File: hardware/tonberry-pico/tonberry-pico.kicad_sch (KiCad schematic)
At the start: 28 parts, among them J1 MicroSD_Breakout, J2 SparkFun I2S Audio Breakout M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, J3 RC522_Breakout, J4 Adafruit_bq25185_5V, J5 UART, J6 WS2812, J7 Buttons, Q1 2N7000, Q2 2N7000, SW1 SW_Push, SW2 SW_Push, SW3 SW_Push, SW4 SW_Push, SW5 SW_Push, U1 Pico

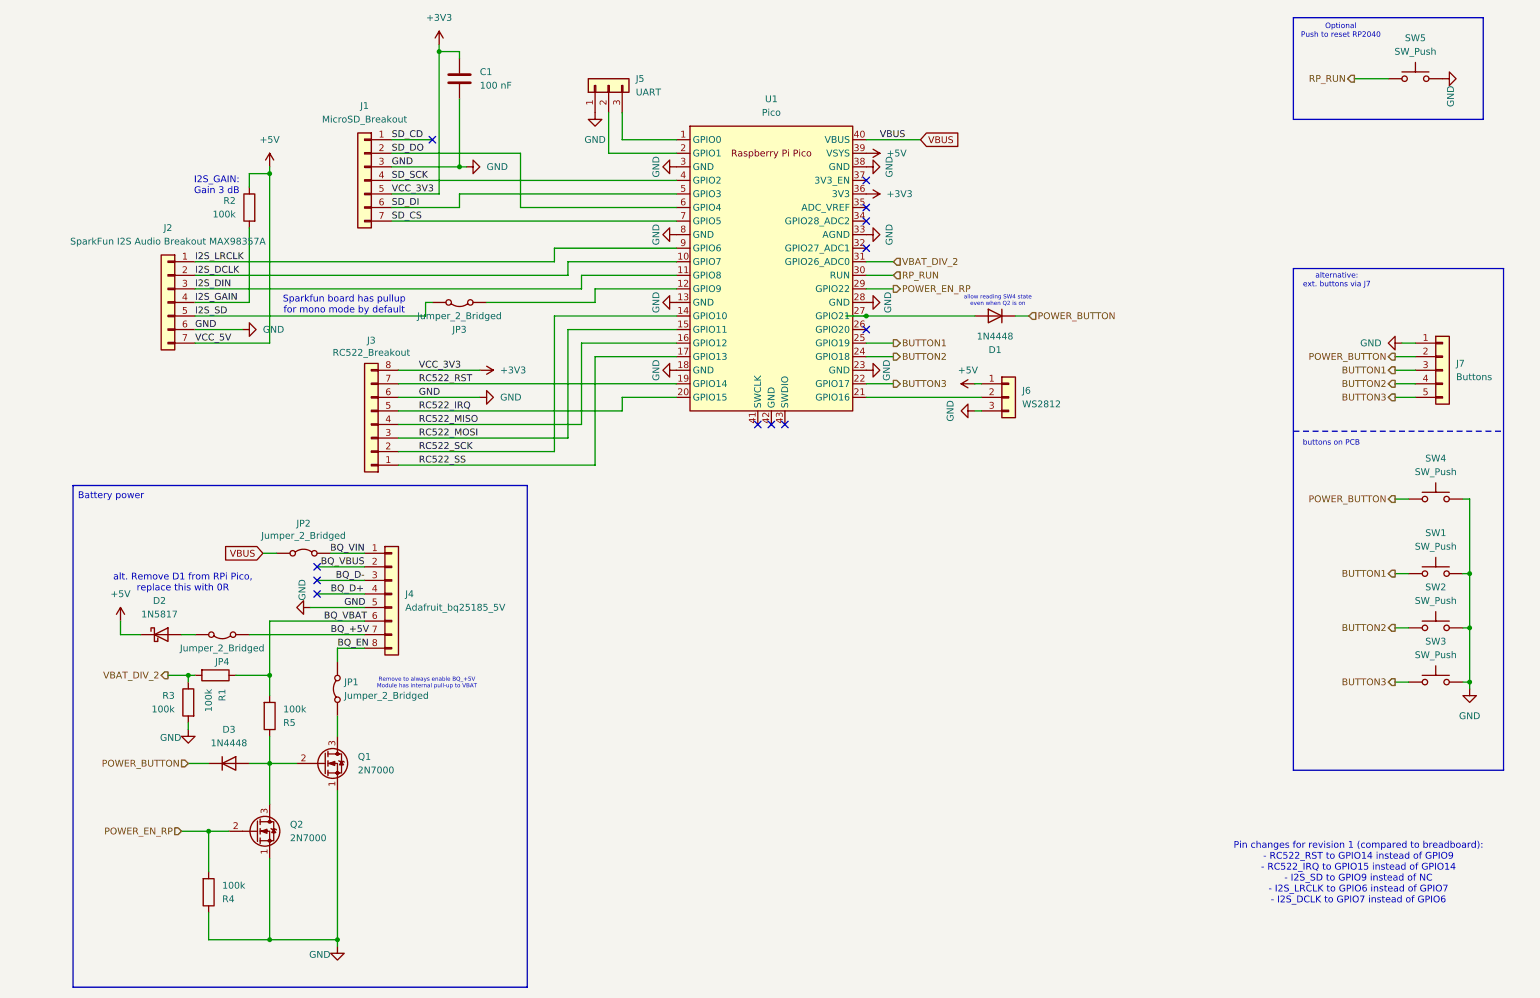
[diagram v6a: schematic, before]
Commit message: hw: Use new and improved RPi Pico symbol in schematic
Signed-off-by: Matthias Blankertz <matthias@blankertz.org>
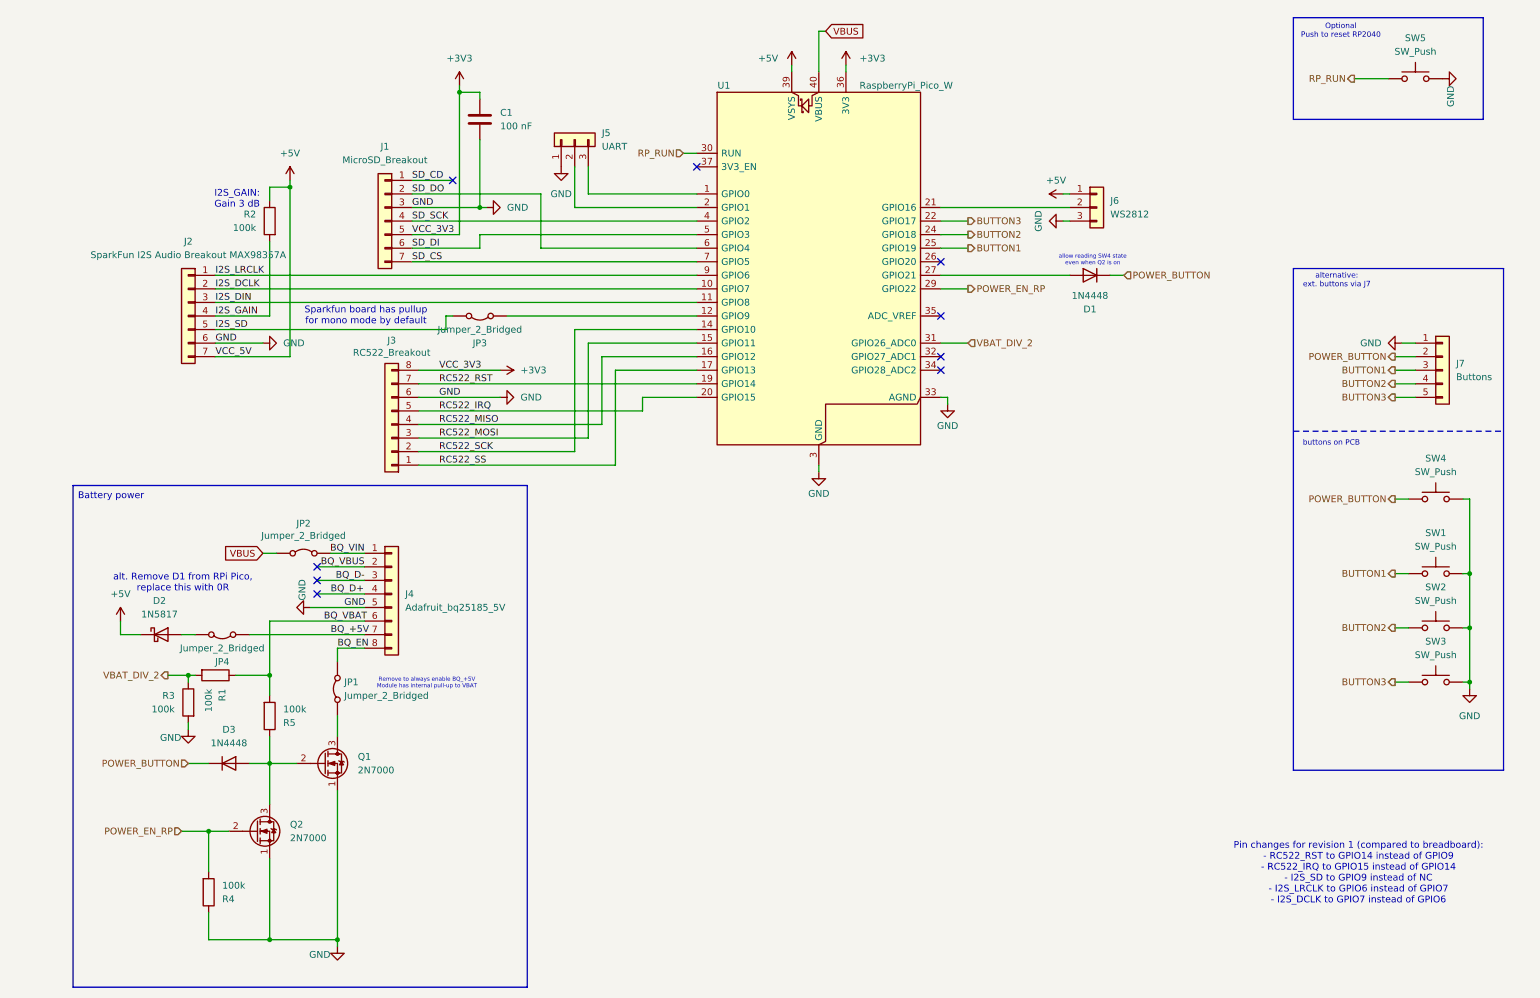
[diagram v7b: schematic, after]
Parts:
- SW5: footprint Button_Switch_THT:Push_E-Switch_KS01Q01 -> Connector_PinHeader_2.54mm:PinHeader_1x02_P2.54mm_Vertical
- U1: value Pico -> RaspberryPi_Pico_W; symbol MCU_RaspberryPi_and_Boards:Pico -> MCU_Module:RaspberryPi_Pico_W
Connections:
- no-connect marks 12 -> 9
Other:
- moved on the sheet: C1, D1, J1, J2, J3, J5, J6, JP3, R2

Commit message: hw: Cleanup schematic style, fix ERC violations
No netlist changes.

Signed-off-by: Matthias Blankertz <matthias@blankertz.org>
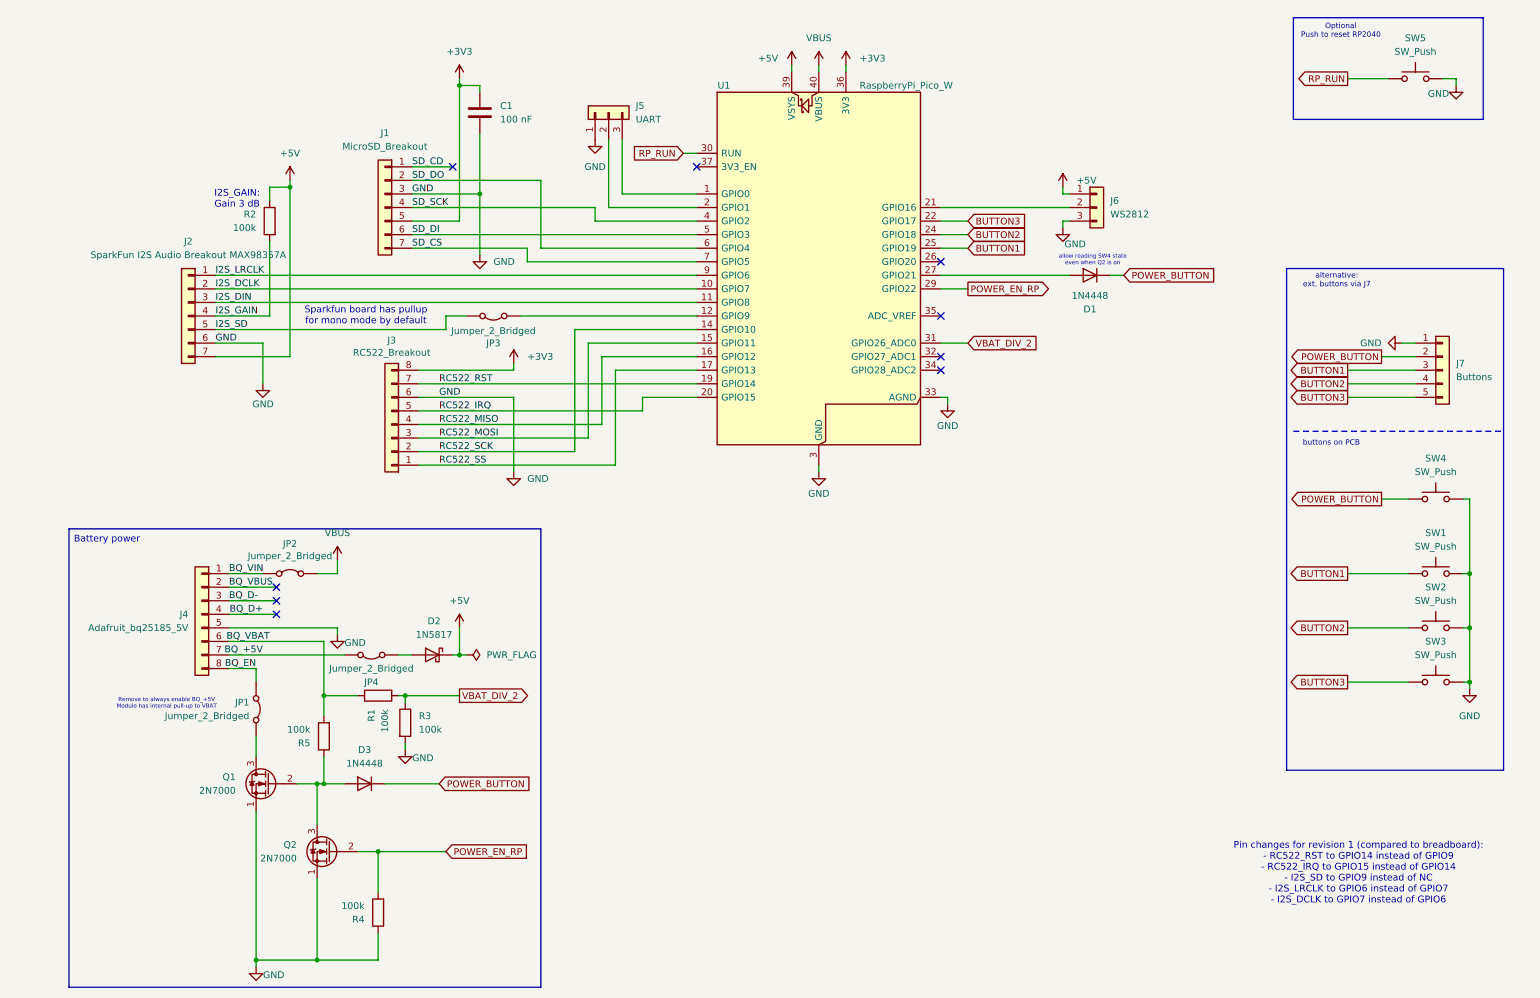
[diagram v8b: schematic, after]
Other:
- note removed: "alt. Remove D1 from RPi Pico, replace this with 0R"
- moved on the sheet: C1, D2, D3, J1, J4, J5, JP1, JP2, JP3, JP4, Q1, Q2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
